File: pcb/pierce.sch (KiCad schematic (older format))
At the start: 81 parts, among them J1 Conn_01x10, J2 Conn_01x10, J3 Trackpoint, SW1 SW_PUSH, SW10 SW_PUSH, SW11 SW_PUSH, SW12 SW_PUSH, SW13 SW_PUSH, SW14 SW_PUSH, SW15 SW_PUSH, SW16 SW_PUSH, SW17 SW_PUSH, SW18 SW_PUSH, SW19 SW_PUSH, SW2 SW_PUSH, SW20 SW_PUSH, SW21 SW_PUSH, SW22 SW_PUSH, SW23 SW_PUSH, SW24 SW_PUSH, SW25 SW_PUSH, SW26 SW_PUSH, SW27 SW_PUSH, SW28 SW_PUSH, SW29 SW_PUSH, SW3 SW_PUSH, SW30 SW_PUSH, SW31 SW_PUSH, SW32 SW_PUSH, SW33 SW_PUSH, SW34 SW_PUSH, SW35 SW_PUSH, SW36 SW_PUSH, SW37 SW_PUSH, SW4 SW_PUSH, SW5 SW_PUSH, SW6 SW_PUSH, SW7 SW_PUSH, SW8 SW_PUSH, SW9 SW_PUSH, U1 ProMicro_r

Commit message: Changed footprint to Elite-C (Reversed for flipped mounting) Changed pins connected to trackpoint to allow USART. (CLK-D5, SDA-D2) Rearranged connection order of trackpoint to match R61 module Cleaner routing
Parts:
- removed U1: ProMicro_r, pierce:ProMicro_v2_1side, symbol kbd:ProMicro_r
- added U1: Elite-C_reverse, pierce:Elite-C_reverse_D5, symbol keebio:Elite-C_reverse
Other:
- moved on the sheet: C1, R1, R2, R3, SW37

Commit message: add connection for rotary encoder
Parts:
- removed J1, J2: Conn_01x10, Connector_IDC:IDC-Header_2x06_P2.54mm_Horizontal, symbol Connector_Generic:Conn_01x10
- added J1, J2: Conn_01x12, Connector_IDC:IDC-Header_2x06_P2.54mm_Horizontal, symbol Connector_Generic:Conn_01x12
- added SW38: Rotary_Encoder, Connector_PinSocket_2.54mm:PinSocket_1x03_P2.54mm_Vertical, symbol Device:Rotary_Encoder
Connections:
- net labels added: GND1, rota, rotal, rotb, rotbl
- wire segments 129 -> 140
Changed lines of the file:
@@
 	8350 1950 8250 1950
 Connection ~ 8250 1950
-$Comp
-L Connector_Generic:Conn_01x10 J1
-U 1 1 6027B116
-P 5750 1150
-F 0 "J1" V 5967 1096 50  0000 C CNN
-F 1 "Conn_01x10" V 5876 1096 50  0000 C CNN
-F 2 "Connector_IDC:IDC-Header_2x06_P2.54mm_Horizontal" H 5750 1150 50  0001 C CNN
-F 3 "~" H 5750 1150 50  0001 C CNN
-	1    5750 1150
-	0    -1   -1   0
-$EndComp
-$Comp
-L Connector_Generic:Conn_01x10 J2
-U 1 1 6027C8CF
-P 5750 3950
-F 0 "J2" V 5967 3896 50  0000 C CNN
-F 1 "Conn_01x10" V 5876 3896 50  0000 C CNN
-F 2 "Connector_IDC:IDC-Header_2x06_P2.54mm_Horizontal" H 5750 3950 50  0001 C CNN
-F 3 "~" H 5750 3950 50  0001 C CNN
-	1    5750 3950
-	0    -1   -1   0
-$EndComp
 Wire Wire Line
 	5350 1350 5350 1550
@@
 Wire Wire Line
 	7450 1300 7450 1950
+$Comp
+L Connector_Generic:Conn_01x12 J1
+U 1 1 603779EC
+P 5850 1150
+F 0 "J1" V 6067 1096 50  0000 C CNN
+F 1 "Conn_01x12" V 5976 1096 50  0000 C CNN
+F 2 "Connector_IDC:IDC-Header_2x06_P2.54mm_Horizontal" H 5850 1150 50  0001 C CNN
+F 3 "~" H 5850 1150 50  0001 C CNN
+	1    5850 1150
+	0    -1   -1   0
+$EndComp
+$Comp
+L Connector_Generic:Conn_01x12 J2
+U 1 1 6038862C
+P 5850 3950
+F 0 "J2" V 6067 3896 50  0000 C CNN
+F 1 "Conn_01x12" V 5976 3896 50  0000 C CNN
+F 2 "Connector_IDC:IDC-Header_2x06_P2.54mm_Horizontal" H 5850 3950 50  0001 C CNN
+F 3 "~" H 5850 3950 50  0001 C CNN
+	1    5850 3950
+	0    -1   -1   0
+$EndComp
+Text GLabel 6350 4350 3    50   Input ~ 0
+rota
+Text GLabel 6450 4350 3    50   Input ~ 0
+rotb
+Wire Wire Line
+	6350 1550 6350 1350
+Wire Wire Line
+	6450 1550 6450 1350
+Wire Wire Line
+	6350 4350 6350 4150
+Wire Wire Line
+	6450 4350 6450 4150
+Text GLabel 9100 4250 2    50   Input ~ 0
+rota
+Text GLabel 9100 4150 2    50   Input ~ 0
+rotb
+Wire Wire Line
+	9100 4150 8950 4150
+Wire Wire Line
+	9100 4250 8950 4250
+Text GLabel 6350 1550 3    50   Input ~ 0
+rotal
+Text GLabel 6450 1550 3    50   Input ~ 0
+rotbl
+Wire Wire Line
+	5950 1550 5950 1350
+$Comp
+L power:GND #PWR0103
+U 1 1 60494EAD
+P 5950 4350
+F 0 "#PWR0103" H 5950 4100 50  0001 C CNN
+F 1 "GND" V 5955 4222 50  0000 R CNN
+F 2 "" H 5950 4350 50  0001 C CNN
+F 3 "" H 5950 4350 50  0001 C CNN
+	1    5950 4350
+	1    0    0    -1
+$EndComp
+Wire Wire Line
+	5950 4350 5950 4150
+$Comp
+L Device:Rotary_Encoder SW38
+U 1 1 604AF34E
+P 5500 2550
+F 0 "SW38" H 5443 2183 50  0000 C CNN
+F 1 "Rotary_Encoder" H 5443 2274 50  0000 C CNN
+F 2 "Connector_PinSocket_2.54mm:PinSocket_1x03_P2.54mm_Vertical" H 5350 2710 50  0001 C CNN
+F 3 "~" H 5500 2810 50  0001 C CNN
+	1    5500 2550
+	-1   0    0    1
+$EndComp
+Text GLabel 5950 2650 2    50   Input ~ 0
+rotal
+Text GLabel 5950 2450 2    50   Input ~ 0
+rotbl
+Wire Wire Line
+	5800 2450 5950 2450
+Wire Wire Line
+	5800 2550 5950 2550
+Wire Wire Line
+	5800 2650 5950 2650
+$Comp
+L power:GND1 #PWR?
+U 1 1 604FF809
+P 5950 1550
+F 0 "#PWR?" H 5950 1300 50  0001 C CNN
+F 1 "GND1" H 5955 1377 50  0000 C CNN
+F 2 "" H 5950 1550 50  0001 C CNN
+F 3 "" H 5950 1550 50  0001 C CNN
+	1    5950 1550
+	1    0    0    -1
+$EndComp
+$Comp
+L power:GND1 #PWR?
+U 1 1 60513148
+P 5950 2550
+F 0 "#PWR?" H 5950 2300 50  0001 C CNN
+F 1 "GND1" V 5955 2422 50  0000 R CNN
+F 2 "" H 5950 2550 50  0001 C CNN
+F 3 "" H 5950 2550 50  0001 C CNN
+	1    5950 2550
+	0    -1   -1   0
+$EndComp
 $EndSCHEMATC

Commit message: small schematics cleanup
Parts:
- SW1, SW10, SW11, SW12, SW13, SW14, SW15, SW16, SW17, SW18, SW19, SW2, SW20, SW21, SW22, SW23, SW24, SW25, SW26, SW27, SW28, SW29, SW3, SW30, SW31, SW32, SW33, SW34, SW35, SW36, SW37, SW4, SW5, SW6, SW7, SW8, SW9: symbol kbd:SW_PUSH -> pierce:SW_PUSH
- U1: symbol keebio:Elite-C_reverse -> pierce:Elite-C_reverse
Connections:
- net col0l: no longer SW1.1, SW2.1
- net col1l: no longer SW8.1, SW9.1
- net col2l: no longer SW15.1, SW16.1, SW17.1
- net col3l: no longer SW23.1, SW24.1, SW25.1
- net col4l: no longer SW30.1, SW31.1, SW32.1
- net col5: no longer SW4.1, SW5.1, SW6.1
- net col6: no longer SW11.1, SW12.1, SW13.1
- net col7: no longer SW19.1, SW20.1, SW21.1
- net col8: no longer SW27.1, SW28.1
- net col9: no longer SW34.1, SW35.1

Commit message: cleanup
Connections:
- net col0l: now also SW1.1, SW2.1
- net col1l: now also SW8.1, SW9.1
- net col2l: now also SW15.1, SW16.1, SW17.1
- net col3l: now also SW23.1, SW24.1, SW25.1
- net col4l: now also SW30.1, SW31.1, SW32.1
- net col5: now also SW4.1, SW5.1, SW6.1
- net col6: now also SW11.1, SW12.1, SW13.1
- net col7: now also SW19.1, SW20.1, SW21.1
- net col8: now also SW27.1, SW28.1
- net col9: now also SW34.1, SW35.1
- no-connect marks 0 -> 4
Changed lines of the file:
@@
 	0    -1   -1   0
 $EndComp
-Wire Wire Line
-	1450 800  1450 2350
-Wire Wire Line
-	2200 800  2200 2350
-Wire Wire Line
-	3700 800  3700 2900
-Wire Wire Line
-	1500 3550 1500 5650
-Wire Wire Line
-	2950 800  2950 2900
-Wire Wire Line
-	4450 800  4450 2900
-Wire Wire Line
-	3000 3550 3000 5650
-Wire Wire Line
-	2250 3550 2250 5650
-Wire Wire Line
-	4500 3550 4500 5100
-Wire Wire Line
-	3750 3550 3750 5100
 Connection ~ 4350 5400
 Wire Wire Line
@@
 	1    0    0    -1
 $EndComp
+Wire Wire Line
+	1450 800  1450 1250
+Connection ~ 1450 1800
+Wire Wire Line
+	1450 1800 1450 2350
+Wire Wire Line
+	1450 1800 1450 1250
+Connection ~ 1450 1250
+Wire Wire Line
+	2200 800  2200 1250
+Connection ~ 2200 1250
+Wire Wire Line
+	2200 1250 2200 1800
+Connection ~ 2200 1800
+Wire Wire Line
+	2200 1800 2200 2350
+Wire Wire Line
+	2950 800  2950 1250
+Connection ~ 2950 1250
+Wire Wire Line
+	2950 1250 2950 1800
+Connection ~ 2950 1800
+Wire Wire Line
+	3700 800  3700 1250
+Connection ~ 3700 1250
+Wire Wire Line
+	4450 800  4450 1250
+Connection ~ 4450 1250
+Wire Wire Line
+	4450 1250 4450 1800
+Connection ~ 4450 1800
+Wire Wire Line
+	4450 1800 4450 2350
+Connection ~ 4450 2350
+Wire Wire Line
+	4450 2350 4450 2900
+Connection ~ 2250 4550
+Wire Wire Line
+	2250 3550 2250 4000
+Connection ~ 2250 4000
+Wire Wire Line
+	2250 4000 2250 4550
+Wire Wire Line
+	1500 3550 1500 4000
+Connection ~ 1500 4000
+Wire Wire Line
+	1500 4000 1500 4550
+Connection ~ 1500 4550
+Wire Wire Line
+	1500 4550 1500 5100
+Connection ~ 1500 5100
+Wire Wire Line
+	1500 5100 1500 5650
+Connection ~ 3750 4550
+Wire Wire Line
+	3750 4550 3750 5100
+Wire Wire Line
+	3750 3550 3750 4000
+Connection ~ 3750 4000
+Wire Wire Line
+	3750 4000 3750 4550
+Wire Wire Line
+	3000 3550 3000 4000
+Connection ~ 3000 4000
+Wire Wire Line
+	3000 4000 3000 4550
+Connection ~ 3000 4550
+Wire Wire Line
+	3000 4550 3000 5100
+Connection ~ 3000 5100
+Wire Wire Line
+	3000 5100 3000 5650
+Wire Wire Line
+	2250 4550 2250 5100
+Connection ~ 2250 5100
+Wire Wire Line
+	2250 5100 2250 5650
+Connection ~ 4500 4550
+Wire Wire Line
+	4500 4550 4500 5100
+Wire Wire Line
+	4500 3550 4500 4000
+Connection ~ 4500 4000
+Wire Wire Line
+	4500 4000 4500 4550
+Wire Wire Line
+	2950 1800 2950 2350
+Connection ~ 2950 2350
+Wire Wire Line
+	2950 2350 2950 2900
+Connection ~ 3700 2350
+Wire Wire Line
+	3700 2350 3700 2900
+Wire Wire Line
+	3700 1250 3700 1800
+Connection ~ 3700 1800
+Wire Wire Line
+	3700 1800 3700 2350
+NoConn ~ 8050 5250
+NoConn ~ 8150 5250
+NoConn ~ 8250 5250
+NoConn ~ 8450 5250
 $EndSCHEMATC

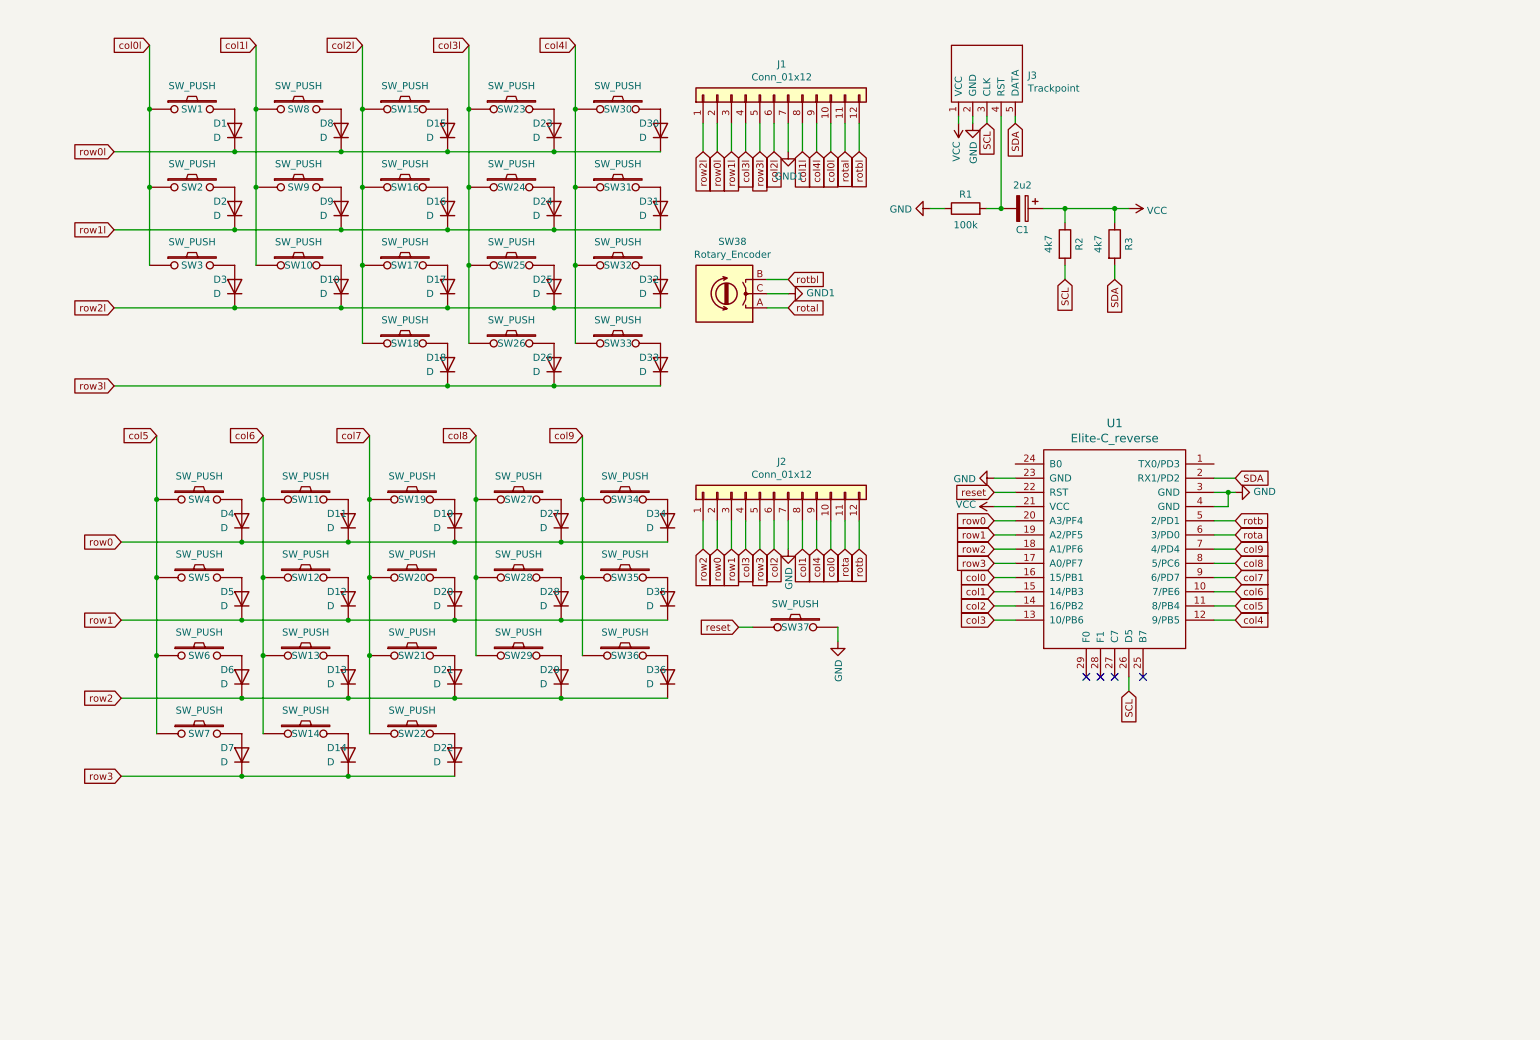
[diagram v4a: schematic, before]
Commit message: adjust schematics for wireless connection between halves
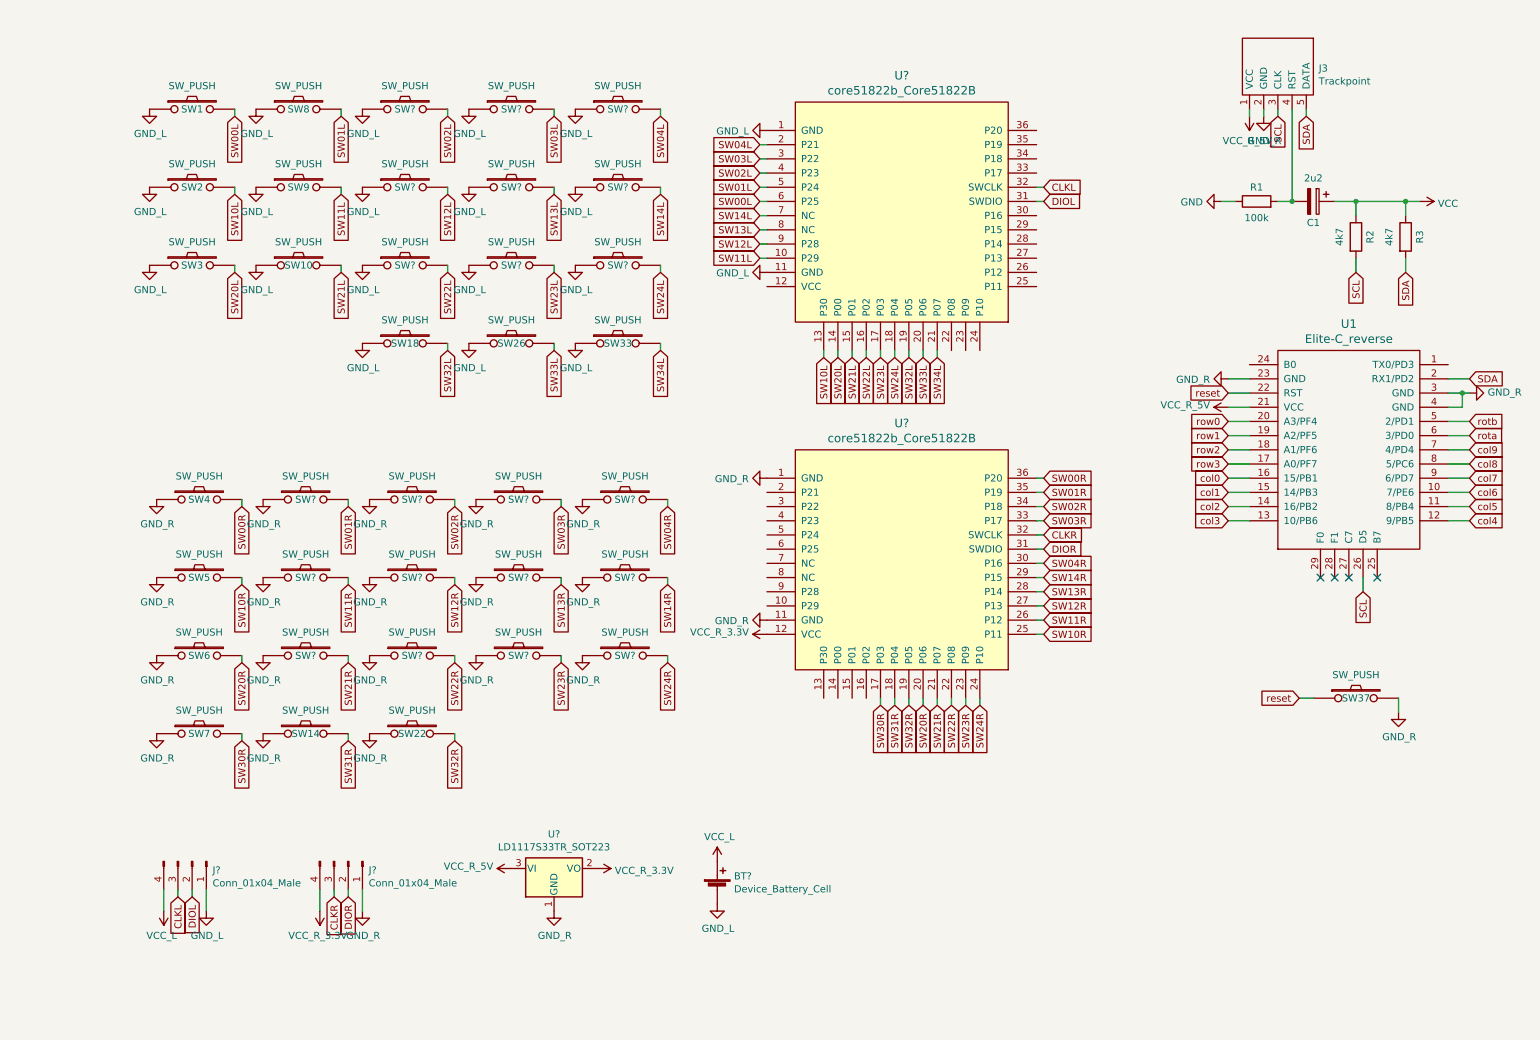
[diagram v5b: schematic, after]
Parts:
- removed D1, D10, D11, D12, D13, D14, D15, D16, D17, D18, D19, D2, D20, D21, D22, D23, D24, D25, D26, D27, D28, D29, D3, D30, D31, D32, D33, D34, D35, D36, D4, D5, D6, D7, D8, D9: D, kbd:D3_SMD_v2, symbol Device:D
- removed J1, J2: Conn_01x12, Connector_IDC:IDC-Header_2x06_P2.54mm_Horizontal, symbol Connector_Generic:Conn_01x12
- removed SW11, SW12, SW13, SW15, SW16, SW17, SW19, SW20, SW21, SW23, SW24, SW25, SW27, SW28, SW29, SW30, SW31, SW32, SW34, SW35, SW36: SW_PUSH, kbd:CherryMX_ChocV2_1u, symbol pierce:SW_PUSH
- removed SW38: Rotary_Encoder, Connector_PinSocket_2.54mm:PinSocket_1x03_P2.54mm_Vertical, symbol Device:Rotary_Encoder
- added BT?: Device_Battery_Cell, symbol pierce:Device_Battery_Cell
- added J? (x2): Conn_01x04_Male, symbol Connector:Conn_01x04_Male
- added SW? (x21): SW_PUSH, kbd:CherryMX_ChocV2_1u, symbol pierce:SW_PUSH
- added U? (x2): core51822b_Core51822B, symbol pierce:core51822b_Core51822B
- added U?: LD1117S33TR_SOT223, Package_TO_SOT_SMD:SOT-223-3_TabPin2, symbol Regulator_Linear:LD1117S33TR_SOT223
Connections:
- net col1l is gone; now on net GND_L: SW10.1, SW8.1, SW9.1
- net col2l is gone; now on net GND_L: SW18.1
- net col3l is gone; now on net GND_L: SW26.1
- net col4l is gone; now on net GND_L: SW33.1
- net GND: no longer J3.2 (GND), SW37.2, U1.23 (GND), U1.3 (GND), U1.4 (GND)
- net VCC: no longer J3.1 (VCC), U1.21 (VCC)
- net col5: no longer SW4.1, SW5.1, SW6.1, SW7.1
- net col6: no longer SW14.1
- net col7: no longer SW22.1
- net SW00L: now reaches SW1.2
- net SW00L: now also U?.6 (P25)
- net SW10L: now reaches SW2.2
- net SW10L: now also U?.13 (P30)
- net SW20L: now reaches SW3.2
- net SW20L: now also U?.14 (P00)
- net SW01L: now reaches SW8.2
- net SW01L: now also U?.5 (P24)
- net SW11L: now reaches SW9.2
- net SW11L: now also U?.10 (P29)
- net SW21L: now reaches SW10.2
- net SW21L: now also U?.15 (P01)
- net SW32L: now reaches SW18.2
- net SW32L: now also U?.19 (P05)
- net SW33L: now reaches SW26.2
- net SW33L: now also U?.20 (P06)
- net SW34L: now reaches SW33.2
- net SW34L: now also U?.21 (P07)
- net SW00R: now reaches SW4.2
- net SW00R: now also U?.36 (P20)
- net SW10R: now reaches SW5.2
- net SW10R: now also U?.25 (P11)
- net SW20R: now reaches SW6.2
- net SW20R: now also U?.20 (P06)
- net SW30R: now reaches SW7.2
- net SW30R: now also U?.17 (P03)
- net SW31R: now reaches SW14.2
- net SW31R: now also U?.18 (P04)
- net SW32R: now reaches SW22.2
- net SW32R: now also U?.19 (P05)
- net col0l renamed GND_L
- net GND_L: now also BT?.2 (-), J?.1 (Pin_1), SW?.1, SW?.1, SW?.1, SW?.1, SW?.1, SW?.1, SW?.1, SW?.1, SW?.1, U?.1 (GND), U?.11 (GND)
- new net CLKL: J?.3 (Pin_3), U?.32 (SWCLK)
- new net CLKR: J?.3 (Pin_3), U?.32 (SWCLK)
- new net DIOL: J?.2 (Pin_2), U?.31 (SWDIO)
- new net DIOR: J?.2 (Pin_2), U?.31 (SWDIO)
- new net GND_R: J3.2 (GND), J?.1 (Pin_1), SW14.1, SW22.1, SW37.2, SW4.1, SW5.1, SW6.1, SW7.1, SW?.1, SW?.1, SW?.1, SW?.1, SW?.1, SW?.1, SW?.1, SW?.1, SW?.1, SW?.1, SW?.1, SW?.1, U1.23 (GND), U1.3 (GND), U1.4 (GND), U?.1 (GND), U?.1 (GND), U?.11 (GND)
- new net SW01R: SW?.2, U?.35 (P19)
- new net SW02L: SW?.2, U?.4 (P23)
- new net SW02R: SW?.2, U?.34 (P18)
- new net SW03L: SW?.2, U?.3 (P22)
- new net SW03R: SW?.2, U?.33 (P17)
- new net SW04L: SW?.2, U?.2 (P21)
- new net SW04R: SW?.2, U?.30 (P16)
- new net SW11R: SW?.2, U?.26 (P12)
- new net SW12L: SW?.2, U?.9 (P28)
- new net SW12R: SW?.2, U?.27 (P13)
- new net SW13L: SW?.2, U?.8 (NC)
- new net SW13R: SW?.2, U?.28 (P14)
- new net SW14L: SW?.2, U?.7 (NC)
- new net SW14R: SW?.2, U?.29 (P15)
- new net SW21R: SW?.2, U?.21 (P07)
- new net SW22L: SW?.2, U?.16 (P02)
- new net SW22R: SW?.2, U?.22 (P08)
- new net SW23L: SW?.2, U?.17 (P03)
- new net SW23R: SW?.2, U?.23 (P09)
- new net SW24L: SW?.2, U?.18 (P04)
- new net SW24R: SW?.2, U?.24 (P10)
- new net VCC_L: BT?.1 (+), J?.4 (Pin_4)
- new net VCC_R_3.3V: J?.4 (Pin_4), U?.12 (VCC), U?.2 (VO)
- new net VCC_R_5V: J3.1 (VCC), U1.21 (VCC), U?.3 (VI)
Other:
- moved on the sheet: C1, J3, R1, R2, R3, SW37, U1
